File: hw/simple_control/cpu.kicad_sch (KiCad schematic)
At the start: 2 parts, among them J4 Raspberry_Pi_0_2_3, U2 Pico

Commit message: [hw] Complete root schematics of simple control
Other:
- company: (none) -> Stefan Misik
- title: (none) -> WS2812 Simple Controller
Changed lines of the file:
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@@
 (kicad_sch (version 20230121) (generator eeschema)
   (paper "A4")
+  (title_block
+    (title "WS2812 Simple Controller")
+    (date "2023-03-09")
+    (company "Stefan Misik")
+    (comment 1 "CPU ")
+  )
   (hierarchical_label "LED_DATA_~{EN}0" (shape output) (at 165.1 104.14 0) (fields_autoplaced)
     (effects (font (size 1.27 1.27)) (justify left))

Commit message: [hw] Add CPU components
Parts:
- added C9: 100n, Capacitor_SMD:C_0805_2012Metric_Pad1.18x1.45mm_HandSolder, symbol Device:C
- added J7: Conn_01x06, Connector_PinSocket_2.54mm:PinSocket_1x06_P2.54mm_Vertical, symbol Connector_Generic:Conn_01x06
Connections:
- net +3.3V: now reaches J4.1 (3V3)
- net +3.3V: now also J4.17 (3V3)
- net +5V: now reaches J4.2 (5V)
- net +5V: now also J4.4 (5V)
- new net +3V3: C9.2, J7.1 (Pin_1)
- new net GND: C9.1, J7.4 (Pin_4)
- new net SPI0_CLK: J7.5 (Pin_5)
- new net SPI0_CS1: J7.2 (Pin_2)
- new net SPI0_MISO: J7.3 (Pin_3)
- new net SPI0_MOSI: J7.6 (Pin_6)
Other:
- added sheet ID EEPROM (id_eeprom.kicad_sch)
- added sheet SPI SD Card (spi_sd_card.kicad_sch)
- added sheet Status LED 0 (status_led.kicad_sch)
- added sheet Status LED 1 (status_led.kicad_sch)
- added sheet Status LED 2 (status_led.kicad_sch)
- added sheet Status LED 3 (status_led.kicad_sch)
- note added: "SPI Flash Module"
- moved on the sheet: U2

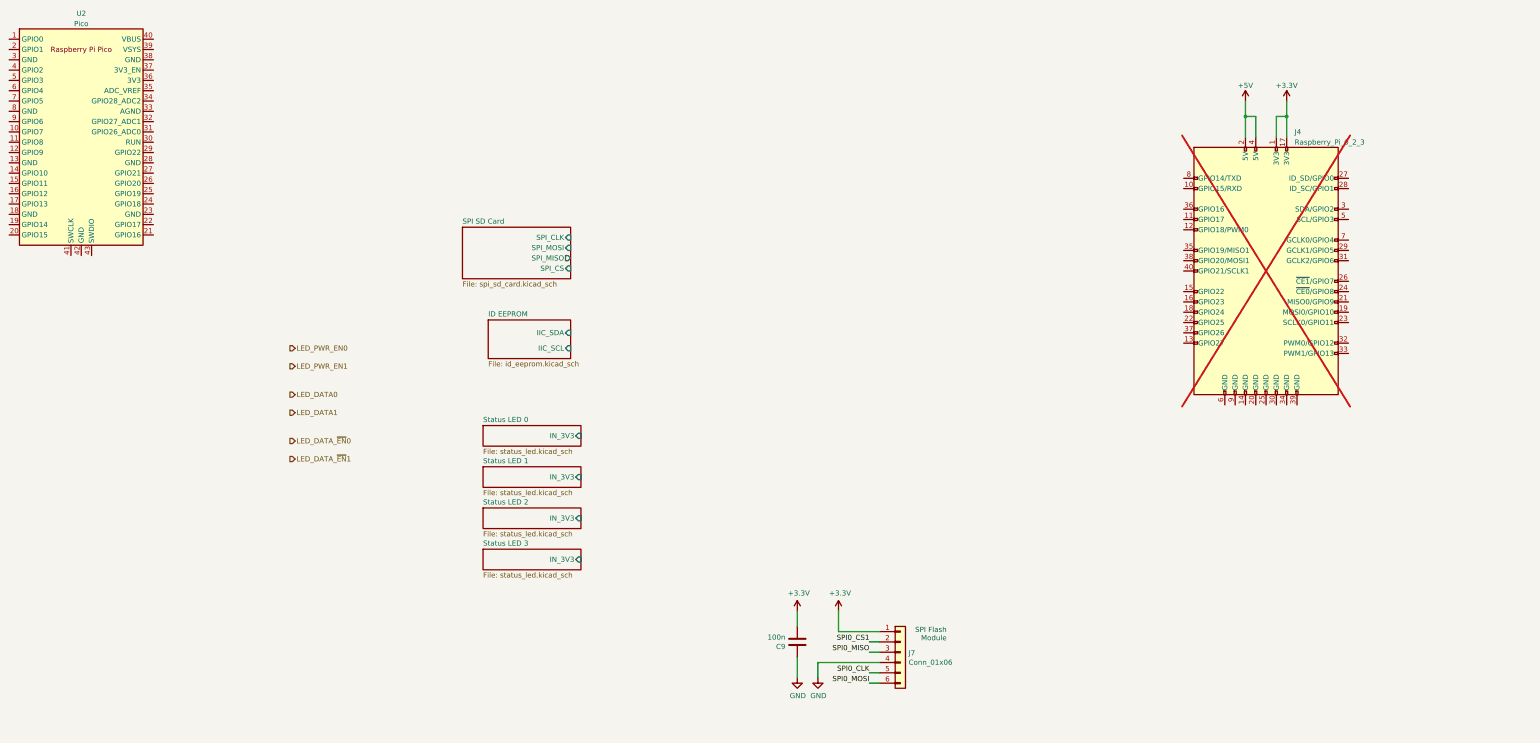
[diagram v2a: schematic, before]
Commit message: [hw] Add CPU modules
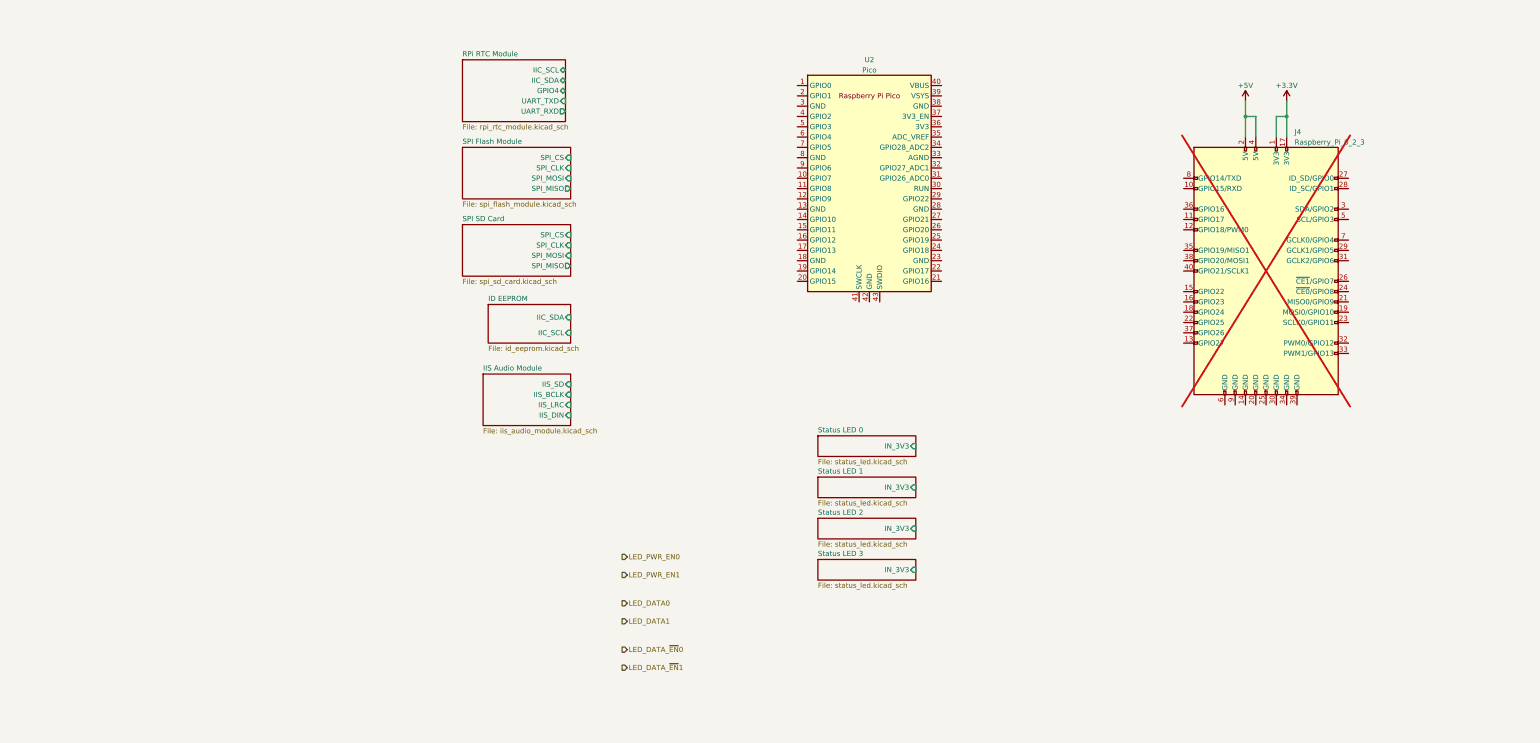
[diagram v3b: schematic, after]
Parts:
- removed C9: 100n, Capacitor_SMD:C_0805_2012Metric_Pad1.18x1.45mm_HandSolder, symbol Device:C
- removed J7: Conn_01x06, Connector_PinSocket_2.54mm:PinSocket_1x06_P2.54mm_Vertical, symbol Connector_Generic:Conn_01x06
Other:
- added sheet IIS Audio Module (iis_audio_module.kicad_sch)
- added sheet RPi RTC Module (rpi_rtc_module.kicad_sch)
- added sheet SPI Flash Module (spi_flash_module.kicad_sch)
- note removed: "SPI Flash Module"
- moved on the sheet: U2

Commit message: [hw] Wire some RPi Pico/Zero connections
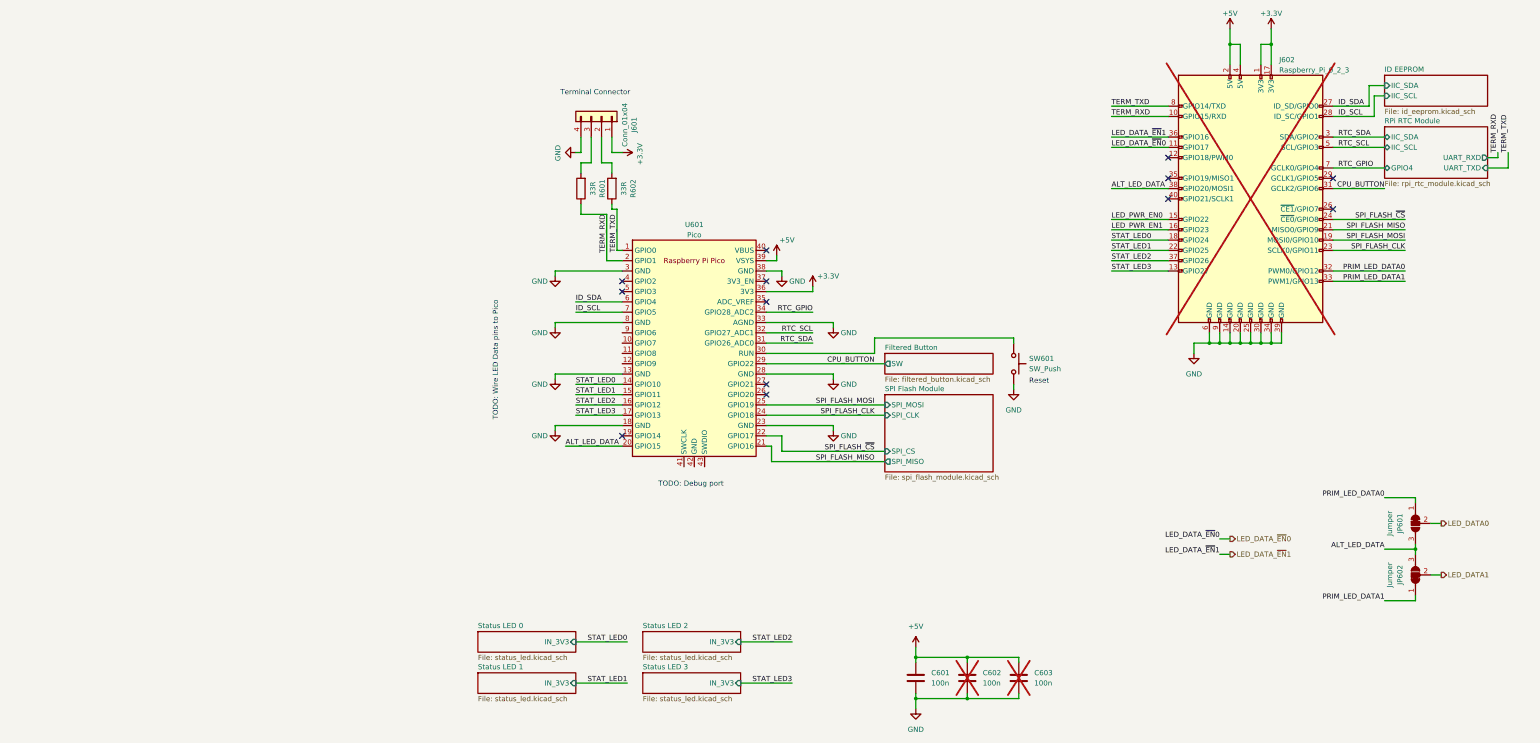
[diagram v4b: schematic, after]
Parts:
- added C601, C602, C603: 100n, symbol Device:C
- added J601: Conn_01x04, Connector_PinHeader_2.54mm:PinHeader_1x04_P2.54mm_Vertical, symbol Connector_Generic:Conn_01x04
- added JP601, JP602: Jumper, symbol Jumper:SolderJumper_3_Bridged12
- added R601, R602: 33R, Resistor_SMD:R_0805_2012Metric_Pad1.20x1.40mm_HandSolder, symbol Device:R
- added SW601: SW_Push, symbol Switch:SW_Push
- renumbered J4 to J602, U2 to U601
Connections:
- net +3.3V: now also U601.36 (3V3), J601.1 (Pin_1)
- net +5V: now also U601.39 (VSYS), C601.1, C602.1, C603.1
- net LED_DATA0: now also JP601.2 (C)
- net LED_DATA1: now also JP602.2 (C)
- net LED_DATA_~{EN}0: now also J602.11 (GPIO17)
- net LED_DATA_~{EN}1: now also J602.36 (GPIO16)
- net LED_PWR_EN0: now also J602.15 (GPIO22)
- net LED_PWR_EN1: now also J602.16 (GPIO23)
- net TERM_TXD: now reaches U601.1 (GPIO0)
- net TERM_TXD: now also J602.8 (GPIO14/TXD), R602.1
- net GND: now reaches U601.13 (GND)
- net GND: now also J602.14 (GND), J602.20 (GND), J602.25 (GND), J602.30 (GND), J602.34 (GND), J602.39 (GND), J602.6 (GND), J602.9 (GND), U601.18 (GND), U601.23 (GND), U601.28 (GND), U601.3 (GND), U601.33 (AGND), U601.38 (GND), U601.8 (GND), C601.2, C602.2, C603.2, J601.4 (Pin_4), SW601.2
- net STAT_LED0: now reaches U601.14 (GPIO10)
- net STAT_LED0: now also J602.18 (GPIO24)
- net STAT_LED1: now reaches U601.15 (GPIO11)
- net STAT_LED1: now also J602.22 (GPIO25)
- net STAT_LED2: now reaches U601.16 (GPIO12)
- net STAT_LED2: now also J602.37 (GPIO26)
- net STAT_LED3: now reaches U601.17 (GPIO13)
- net STAT_LED3: now also J602.13 (GPIO27)
- net TERM_RXD: now reaches U601.2 (GPIO1)
- net TERM_RXD: now also J602.10 (GPIO15/RXD), R601.1
- net ALT_LED_DATA: now reaches U601.20 (GPIO15)
- net ALT_LED_DATA: now also J602.38 (GPIO20/MOSI1), JP601.3 (B), JP602.3 (B)
- net SPI_FLASH_MISO: now reaches U601.21 (GPIO16)
- net SPI_FLASH_MISO: now also J602.21 (MISO0/GPIO9)
- net SPI_FLASH_~{CS}: now reaches U601.22 (GPIO17)
- net SPI_FLASH_~{CS}: now also J602.24 (~{CE0}/GPIO8)
- net SPI_FLASH_CLK: now reaches U601.24 (GPIO18)
- net SPI_FLASH_CLK: now also J602.23 (SCLK0/GPIO11)
- net SPI_FLASH_MOSI: now reaches U601.25 (GPIO19)
- net SPI_FLASH_MOSI: now also J602.19 (MOSI0/GPIO10)
- net CPU_BUTTON: now reaches U601.29 (GPIO22)
- net CPU_BUTTON: now also J602.31 (GCLK2/GPIO6)
- net at U601.30 (RUN): now also SW601.1
- net RTC_SDA: now reaches U601.31 (GPIO26_ADC0)
- net RTC_SDA: now also J602.3 (SDA/GPIO2)
- net RTC_SCL: now reaches U601.32 (GPIO27_ADC1)
- net RTC_SCL: now also J602.5 (SCL/GPIO3)
- net RTC_GPIO: now reaches U601.34 (GPIO28_ADC2)
- net RTC_GPIO: now also J602.7 (GCLK0/GPIO4)
- net ID_SDA: now reaches U601.6 (GPIO4)
- net ID_SDA: now also J602.27 (ID_SD/GPIO0)
- net ID_SCL: now reaches U601.7 (GPIO5)
- net ID_SCL: now also J602.28 (ID_SC/GPIO1)
- net PRIM_LED_DATA0: now reaches J602.32 (PWM0/GPIO12)
- net PRIM_LED_DATA0: now also JP601.1 (A)
- net PRIM_LED_DATA1: now reaches J602.33 (PWM1/GPIO13)
- net PRIM_LED_DATA1: now also JP602.1 (A)
- new net: J601.2 (Pin_2), R602.2
- new net: J601.3 (Pin_3), R601.2
- no-connect marks 0 -> 13
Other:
- removed sheet IIS Audio Module
- removed sheet SPI SD Card
- added sheet Filtered Button (filtered_button.kicad_sch)
- note added: "Reset"
- note added: "TODO: Debug port"
- note added: "TODO: Wire LED Data pins to Pico"
- note added: "Terminal Connector"
- moved on the sheet: J602, U601

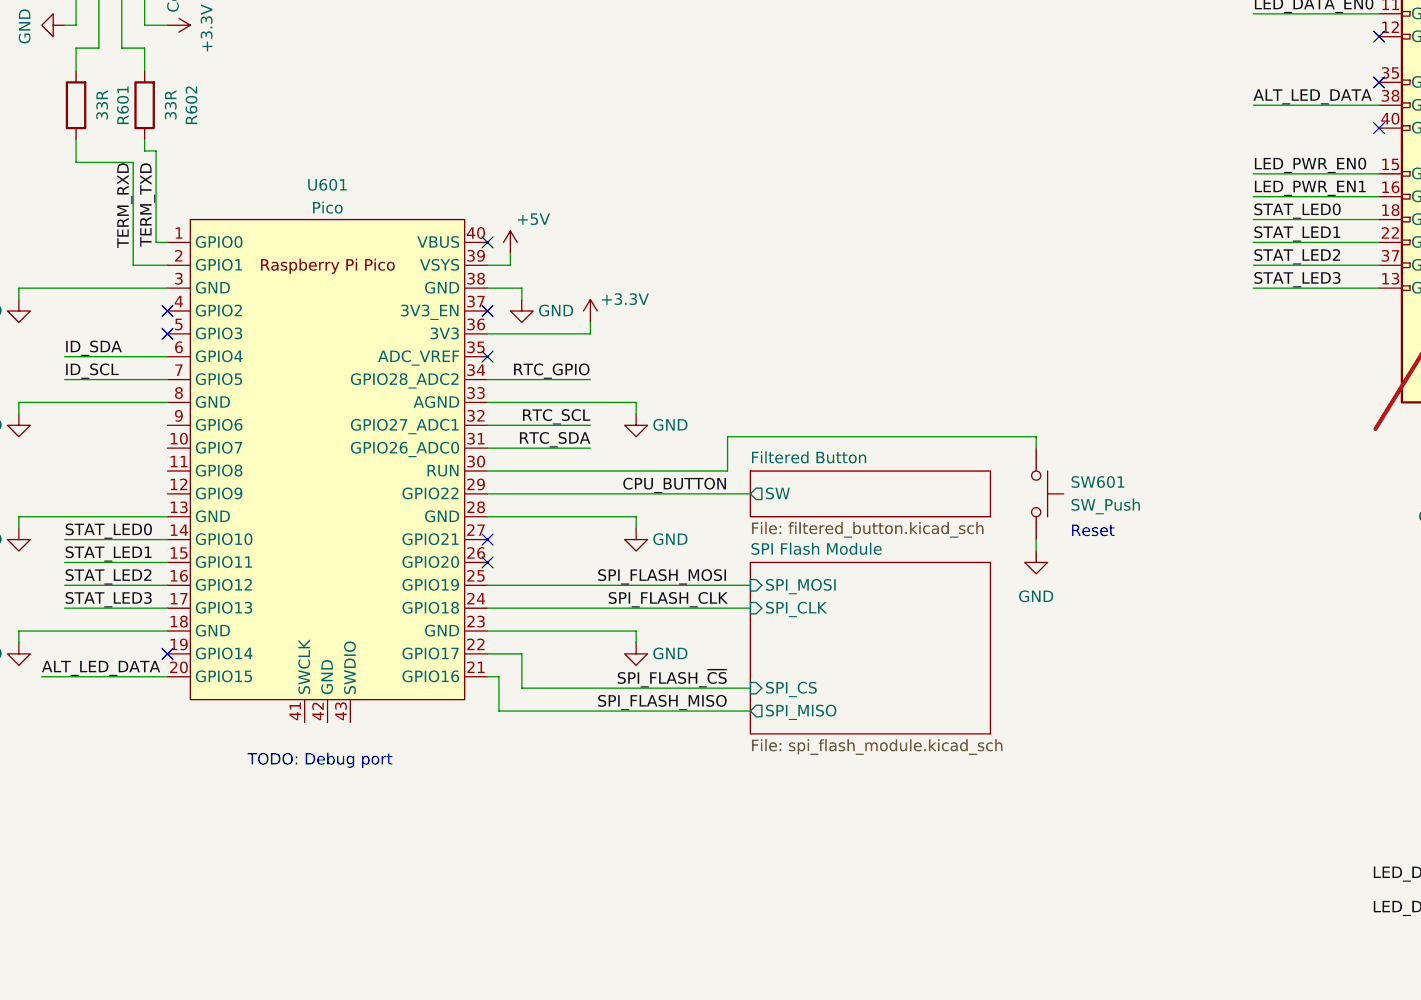
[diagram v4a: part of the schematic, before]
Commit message: [hw] Fix ERC issues, update RPi Pico library
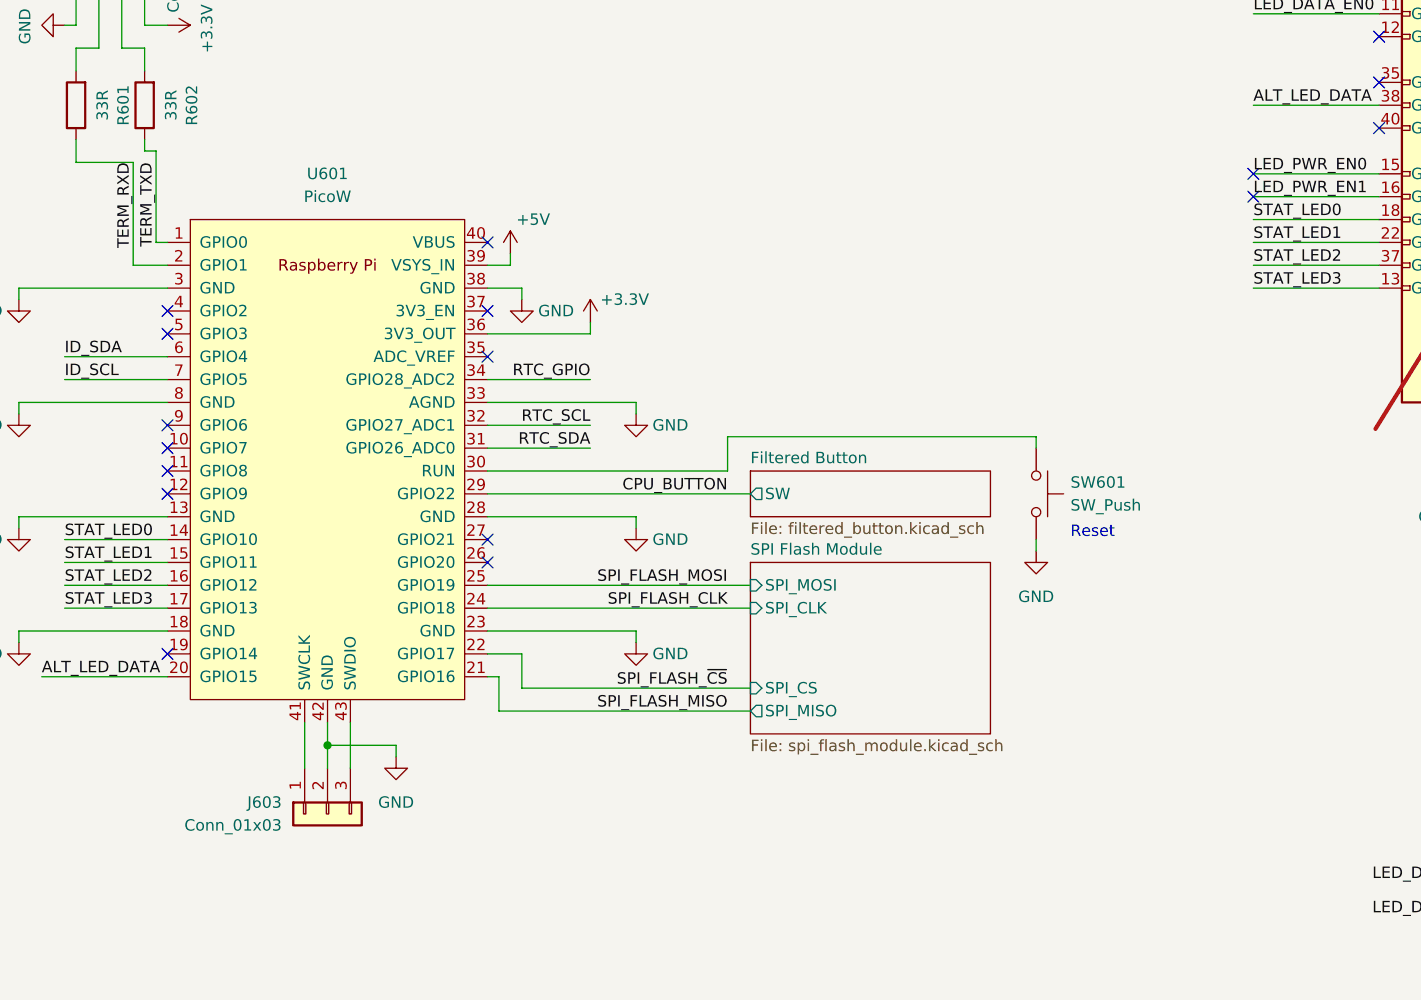
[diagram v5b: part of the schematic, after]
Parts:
- removed U601: Pico, RPi_Pico:RPi_Pico_SMD_TH, symbol rp-pico:Pico
- added J603: Conn_01x03, symbol Connector_Generic:Conn_01x03
- added U601: PicoW, RPi_PicoW:RPi_Pico_SMD_TH, symbol rp-pico:PicoW
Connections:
- net +3.3V: now also U601.36 (3V3)
- net +5V: now also U601.39 (VSYS)
- net ALT_LED_DATA: now also U601.20 (GPIO15)
- net CPU_BUTTON: now also U601.29 (GPIO22)
- net GND: now also J603.2 (Pin_2), U601.13 (GND), U601.18 (GND), U601.23 (GND), U601.28 (GND), U601.3 (GND), U601.33 (AGND), U601.38 (GND), U601.42 (GND), U601.8 (GND)
- net ID_SCL: now also U601.7 (GPIO5)
- net ID_SDA: now also U601.6 (GPIO4)
- net RTC_GPIO: now also U601.34 (GPIO28_ADC2)
- net RTC_SCL: now also U601.32 (GPIO27_ADC1)
- net RTC_SDA: now also U601.31 (GPIO26_ADC0)
- net SPI_FLASH_CLK: now also U601.24 (GPIO18)
- net SPI_FLASH_MISO: now also U601.21 (GPIO16)
- net SPI_FLASH_MOSI: now also U601.25 (GPIO19)
- net SPI_FLASH_~{CS}: now also U601.22 (GPIO17)
- net STAT_LED0: now also U601.14 (GPIO10)
- net STAT_LED1: now also U601.15 (GPIO11)
- net STAT_LED2: now also U601.16 (GPIO12)
- net STAT_LED3: now also U601.17 (GPIO13)
- net TERM_RXD: now also U601.2 (GPIO1)
- net TERM_TXD: now also U601.1 (GPIO0)
- net at SW601.1: now also U601.30 (RUN)
- new net: J603.1 (Pin_1), U601.41 (SWCLK)
- new net: J603.3 (Pin_3), U601.43 (SWDIO)
- no-connect marks 13 -> 19
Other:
- note removed: "TODO: Debug port"
